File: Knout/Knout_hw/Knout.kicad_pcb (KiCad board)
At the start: 4 copper layers, 118 x 21.4 mm, 88 parts, among them Q1 IRF9317, Q2 2N7002, Q3 2N7002, Q4 IRLML9303, Q6 BC848, Q7 IRLML6401, SW1 BUTTON_H

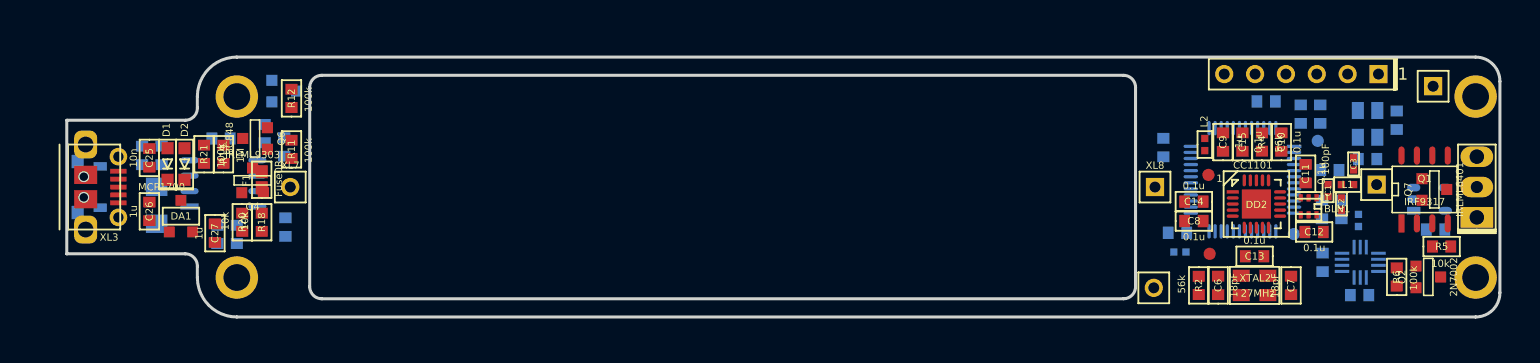
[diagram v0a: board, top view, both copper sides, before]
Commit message: + Snake fw started
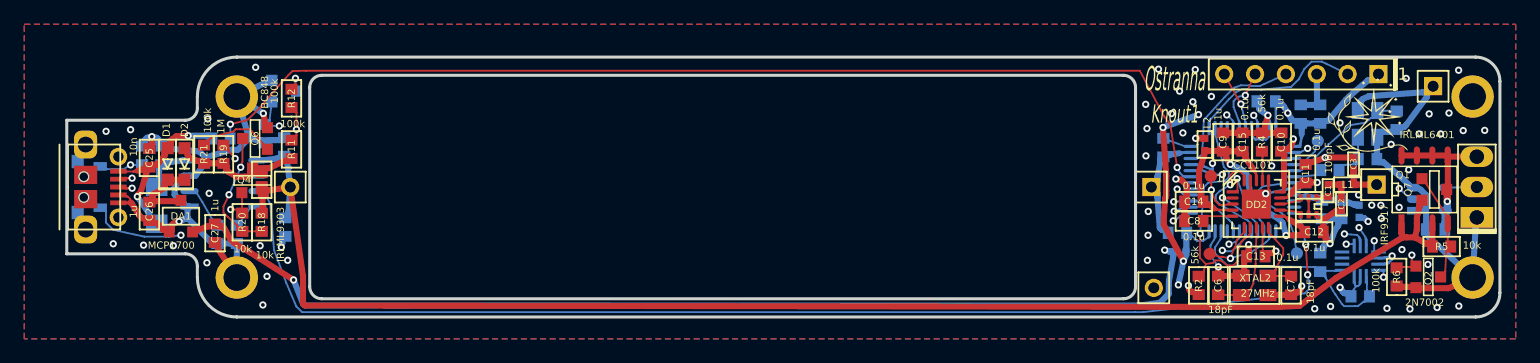
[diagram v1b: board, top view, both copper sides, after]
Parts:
- Logo1: footprint Pictures:Ostranna_12d7_10d1 -> Pictures:Ostranna_8x8; moved to F.Cu
- moved Logo1 110.1 mm to (198.6, 94.3), turned to 0 degrees
- moved TP3 1.61 mm to (192.3, 105.5)
- moved L4 0.75 mm to (197.4, 102.0)
- moved XL8 0.30 mm to (180.3, 100.0)
- moved HOLE2 0.25 mm to (206.8, 92.5)
- moved HOLE4 0.25 mm to (206.8, 107.5)
- moved TP2 0.22 mm to (185.2, 99.1)
- moved C17 0.20 mm to (194.2, 106.2)
- moved C16 0.11 mm to (197.5, 109.0)
- moved DD3 0.10 mm to (197.5, 106.1)
- moved C13 0.10 mm to (188.9, 105.7)
- turned R1 to 0 degrees
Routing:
- net GND: track 0.00 -> 329.8 mm, vias 0 -> 65
- net /BAT_IN: track 0.00 -> 123.2 mm
- net /USB_DM: track 0.00 -> 104.4 mm, vias 0 -> 2
- net /USB_DP: track 0.00 -> 102.6 mm, vias 0 -> 2
- net /IS_CHARGING: track 0.00 -> 101.1 mm, vias 0 -> 2
- net /ADC_BAT_EN: track 0.00 -> 99.9 mm, vias 0 -> 2
- net +3v3: track 0.00 -> 99.2 mm, vias 0 -> 3
- net /ADC_BAT: track 0.00 -> 98.4 mm, vias 0 -> 2
- net Net-(DD1-Pad31): track 0.00 -> 88.0 mm, vias 0 -> 2
- net PwrMCU: track 0.00 -> 70.9 mm, vias 0 -> 6
- net VCC: track 0.00 -> 62.7 mm, vias 0 -> 6
- net /NPX_PWR_EN: track 0.00 -> 24.3 mm, vias 0 -> 2
- net /ACC_PWR: track 0.00 -> 20.6 mm
- net /CC_CS: track 0.00 -> 20.5 mm, vias 0 -> 1
- net /ACC_MISO: track 0.00 -> 19.6 mm, vias 0 -> 2
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- added copper zone on B.Cu, net GND
- added copper zone on F.Cu, net GND
- added copper zone on In1.Cu, net GND
- added copper zone on In2.Cu, net GND
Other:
- board text added: "Knout1"
- board text removed: "Snake v1"
